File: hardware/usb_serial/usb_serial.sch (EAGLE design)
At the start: 16 parts, among them J1 MICRO-USB

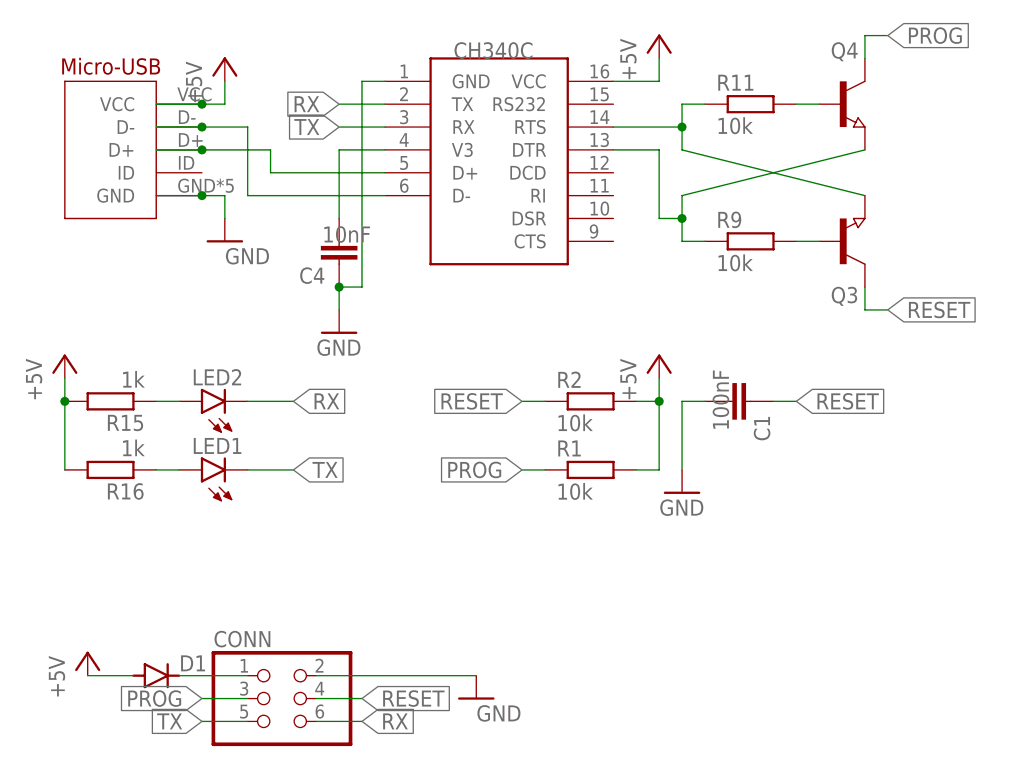
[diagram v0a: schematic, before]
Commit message: Migrated back to ESP32, updated pins in code and updated hardware, also updated readme
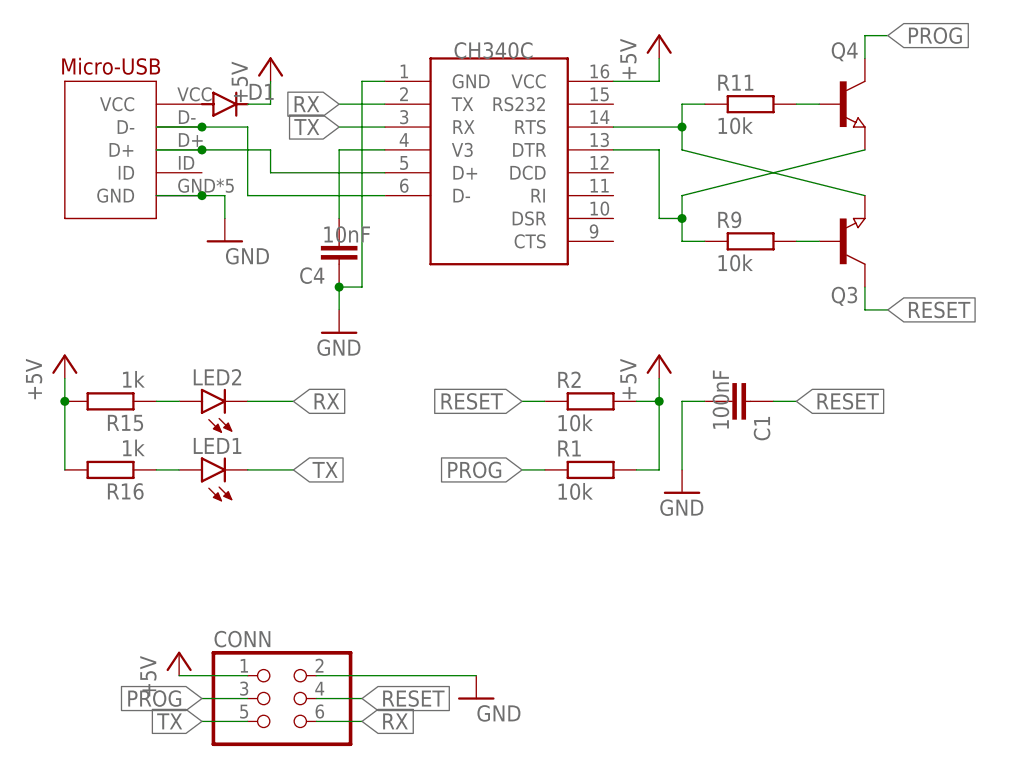
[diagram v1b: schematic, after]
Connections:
- net +5V: now also CONN.1, D1.C; no longer D1.A, J1.VCC
- net N$1: now also D1.A, J1.VCC; no longer CONN.1, D1.C
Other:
- moved on the sheet: D1
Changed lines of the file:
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@@
 <attribute name="VALUE" x="27.94" y="15.24" size="1.778" layer="96"/>
 </instance>
-<instance part="P+4" gate="1" x="-30.48" y="15.24" smashed="yes" grouprefs="USB-INTERFACE">
-<attribute name="VALUE" x="-33.02" y="10.16" size="1.778" layer="96" rot="R90"/>
+<instance part="P+4" gate="1" x="-25.4" y="15.24" smashed="yes" grouprefs="USB-INTERFACE">
+<attribute name="VALUE" x="-27.94" y="10.16" size="1.778" layer="96" rot="R90"/>
 </instance>
 <instance part="GND8" gate="1" x="-30.48" y="-5.08" smashed="yes" grouprefs="USB-INTERFACE">
@@
 <attribute name="VALUE" x="-50.8" y="-22.86" size="1.778" layer="96" rot="R90"/>
 </instance>
-<instance part="P+2" gate="1" x="-45.72" y="-50.8" smashed="yes" grouprefs="CONNECTOR">
-<attribute name="VALUE" x="-48.26" y="-55.88" size="1.778" layer="96" rot="R90"/>
+<instance part="P+2" gate="1" x="-35.56" y="-50.8" smashed="yes" grouprefs="CONNECTOR">
+<attribute name="VALUE" x="-38.1" y="-55.88" size="1.778" layer="96" rot="R90"/>
 </instance>
 <instance part="GND1" gate="1" x="-2.54" y="-55.88" smashed="yes" grouprefs="CONNECTOR">
@@
 <attribute name="VALUE" x="23.749" y="-19.304" size="1.778" layer="96" rot="R270"/>
 </instance>
-<instance part="D1" gate="G$1" x="-38.1" y="-53.34" smashed="yes">
-<attribute name="NAME" x="-35.56" y="-52.8574" size="1.778" layer="95"/>
-<attribute name="VALUE" x="-35.56" y="-55.6514" size="1.778" layer="96"/>
+<instance part="D1" gate="G$1" x="-30.48" y="10.16" smashed="yes">
+<attribute name="NAME" x="-27.94" y="10.6426" size="1.778" layer="95"/>
+<attribute name="VALUE" x="-27.94" y="7.8486" size="1.778" layer="96"/>
 </instance>
 <instance part="P+3" gate="1" x="17.78" y="-17.78" smashed="yes">
@@
 <net name="+5V" class="0">
 <segment>
-<wire x1="-38.1" y1="10.16" x2="-33.02" y2="10.16" width="0.1524" layer="91" grouprefs="USB-INTERFACE"/>
-<pinref part="P+4" gate="1" pin="+5V"/>
-<wire x1="-33.02" y1="10.16" x2="-30.48" y2="10.16" width="0.1524" layer="91" grouprefs="USB-INTERFACE"/>
-<wire x1="-30.48" y1="10.16" x2="-30.48" y2="12.7" width="0.1524" layer="91" grouprefs="USB-INTERFACE"/>
-<pinref part="J1" gate="A" pin="VCC"/>
-<junction x="-33.02" y="10.16"/>
-</segment>
-<segment>
 <pinref part="U$3" gate="G$1" pin="VCC"/>
 <wire x1="12.7" y1="12.7" x2="17.78" y2="12.7" width="0.1524" layer="91" grouprefs="USB-INTERFACE"/>
@@
 <junction x="-48.26" y="-22.86"/>
 <pinref part="P+1" gate="1" pin="+5V"/>
-</segment>
-<segment>
-<pinref part="P+2" gate="1" pin="+5V"/>
-<pinref part="D1" gate="G$1" pin="A"/>
-<wire x1="-45.72" y1="-53.34" x2="-40.64" y2="-53.34" width="0.1524" layer="91"/>
 </segment>
 <segment>
@@
 <wire x1="17.78" y1="-22.86" x2="17.78" y2="-20.32" width="0.1524" layer="91"/>
 <junction x="17.78" y="-22.86"/>
+</segment>
+<segment>
+<pinref part="P+2" gate="1" pin="+5V"/>
+<pinref part="CONN" gate="A" pin="1"/>
+<wire x1="-35.56" y1="-53.34" x2="-27.94" y2="-53.34" width="0.1524" layer="91"/>
+</segment>
+<segment>
+<pinref part="D1" gate="G$1" pin="C"/>
+<wire x1="-27.94" y1="10.16" x2="-25.4" y2="10.16" width="0.1524" layer="91"/>
+<pinref part="P+4" gate="1" pin="+5V"/>
+<wire x1="-25.4" y1="10.16" x2="-25.4" y2="12.7" width="0.1524" layer="91"/>
 </segment>
 </net>
@@
 <net name="N$1" class="0">
 <segment>
-<pinref part="D1" gate="G$1" pin="C"/>
-<pinref part="CONN" gate="A" pin="1"/>
-<wire x1="-35.56" y1="-53.34" x2="-27.94" y2="-53.34" width="0.1524" layer="91"/>
-</segment>
-</net>
+<pinref part="J1" gate="A" pin="VCC"/>
+<pinref part="D1" gate="G$1" pin="A"/>
+</segment>
+</net>
